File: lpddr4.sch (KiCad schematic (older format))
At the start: 41 parts

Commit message: Connect power supplies and CHANNEL A signals to edge connector
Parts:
- removed R?: R_240R_0402, lpddr4-testbed-footprints:0402-res, symbol lpddr4-testbed:R_240R_0402
- removed R? (x7): R_40R2_0402, lpddr4-testbed-footprints:0402-res, symbol lpddr4-testbed:R_40R2_0402
- removed R?: R_0R_0402, lpddr4-testbed-footprints:0402-res, symbol lpddr4-testbed:R_0R_0402
- gave numbers to parts that had none: 31
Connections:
- net labels removed: CA0_B, CA1_B, CA2_B, CA3_B, CA4_B, CA5_B, CKE0_B, DM2_N, DM3_N, DQ16, DQ17, DQ18, DQ19, DQ20, DQ21, DQ22, DQ23, DQ24, DQ25, DQ26, DQ27, DQ28, DQ29, DQ30, DQ31, DQS2_C, DQS2_T, DQS3_C, DQS3_T, ODT0_B, ODT1
- wire segments 190 -> 114

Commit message: Connect signals to DDR CHANNEL A
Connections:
- net labels added: CA_0A, CA_1A, CK_CA, CK_TA, CS0_A, DMI_0A, DMI_1A, DQ00_A, DQ01_A, DQ02_A, DQ03_A, DQ04_A, DQ05_A, DQ06_A, DQ07_A, DQ08_A, DQ09_A, DQ10_A, DQ11_A, DQ12_A, DQ13_A, DQ14_A, DQ15_A, DQ_S0_CA, DQ_S0_TA, DQ_S1_CA, DQ_S1_TA, VDD1, VDD2, VDDQ
- net labels removed: DM0_N, DM1_N, DQ00, DQ01, DQ02, DQ03, DQ04, DQ05, DQ06, DQ07, DQ08, DQ09, DQ10, DQ11, DQ12, DQ13, DQ14, DQ15, DQS0_C, DQS0_T, DQS1_C, DQS1_T
- wire segments 114 -> 120
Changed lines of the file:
@@
 $EndDescr
 Wire Wire Line
-	4650 5550 4650 5850
+	4650 5550 4650 5625
 $Comp
 L lpddr4-testbed:GND #PWR01
 U 1 1 6041895C
-P 4650 5850
-F 0 "#PWR01" H 4650 5600 50  0001 C CNN
-F 1 "GND" H 4655 5677 50  0000 C CNN
-F 2 "" H 4650 5850 50  0001 C CNN
-F 3 "" H 4650 5850 50  0001 C CNN
-	1    4650 5850
-	1    0    0    -1
-$EndComp
-Wire Wire Line
-	10900 5550 10900 5850
+P 4650 5625
+F 0 "#PWR01" H 4650 5375 50  0001 C CNN
+F 1 "GND" H 4655 5452 50  0000 C CNN
+F 2 "" H 4650 5625 50  0001 C CNN
+F 3 "" H 4650 5625 50  0001 C CNN
+	1    4650 5625
+	1    0    0    -1
+$EndComp
+Wire Wire Line
+	10900 5550 10900 5650
 $Comp
 L lpddr4-testbed:GND #PWR09
 U 1 1 6042116F
-P 10900 5850
-F 0 "#PWR09" H 10900 5600 50  0001 C CNN
-F 1 "GND" H 10905 5677 50  0000 C CNN
-F 2 "" H 10900 5850 50  0001 C CNN
-F 3 "" H 10900 5850 50  0001 C CNN
-	1    10900 5850
-	1    0    0    -1
-$EndComp
-Text Label 3050 4550 0    50   ~ 0
-DQ01
-Wire Wire Line
-	3050 4550 3850 4550
-Wire Wire Line
-	3050 4750 3850 4750
-Wire Wire Line
-	3050 4950 3850 4950
-Wire Wire Line
-	3850 5150 3050 5150
-Text Label 3050 4750 0    50   ~ 0
-DQ03
-Text Label 3050 4950 0    50   ~ 0
-DQ05
-Text Label 3050 5150 0    50   ~ 0
-DQ07
-Wire Wire Line
-	3850 4450 3050 4450
-Wire Wire Line
-	3850 4650 3050 4650
-Wire Wire Line
-	3850 4850 3050 4850
-Wire Wire Line
-	3850 5050 3050 5050
-Text Label 3050 4650 0    50   ~ 0
-DQ02
-Text Label 3050 4850 0    50   ~ 0
-DQ04
-Text Label 3050 5050 0    50   ~ 0
-DQ06
-Text Label 3050 4450 0    50   ~ 0
-DQ00
-Text Label 6250 5050 2    50   ~ 0
-DQ14
-Wire Wire Line
-	6250 5050 5450 5050
-Wire Wire Line
-	6250 4850 5450 4850
-Wire Wire Line
-	6250 4650 5450 4650
-Wire Wire Line
-	5450 4450 6250 4450
-Text Label 6250 4650 2    50   ~ 0
-DQ10
-Text Label 6250 4450 2    50   ~ 0
-DQ08
-Wire Wire Line
-	5450 5150 6250 5150
-Wire Wire Line
-	5450 4950 6250 4950
-Wire Wire Line
-	5450 4750 6250 4750
-Wire Wire Line
-	5450 4550 6250 4550
-Text Label 6250 4950 2    50   ~ 0
-DQ13
-Text Label 6250 4750 2    50   ~ 0
-DQ11
-Text Label 6250 4550 2    50   ~ 0
-DQ09
-Text Label 6250 5150 2    50   ~ 0
-DQ15
-Wire Wire Line
-	3050 4250 3850 4250
-Wire Wire Line
-	3850 4350 3050 4350
-Text Label 3050 4350 0    50   ~ 0
-DQS0_C
-Text Label 3050 4250 0    50   ~ 0
-DQS0_T
-Wire Wire Line
-	6250 4250 5450 4250
-Wire Wire Line
-	5450 4350 6250 4350
-Text Label 6250 4350 2    50   ~ 0
-DQS1_C
-Wire Wire Line
-	3850 5250 3050 5250
-Text Label 3050 5250 0    50   ~ 0
-DM0_N
-Wire Wire Line
-	5450 5250 6250 5250
-Text Label 6250 5250 2    50   ~ 0
-DM1_N
-Wire Wire Line
-	3850 3050 3050 3050
-Text Label 3050 3050 0    50   ~ 0
-CS0_N_A
+P 10900 5650
+F 0 "#PWR09" H 10900 5400 50  0001 C CNN
+F 1 "GND" H 10905 5477 50  0000 C CNN
+F 2 "" H 10900 5650 50  0001 C CNN
+F 3 "" H 10900 5650 50  0001 C CNN
+	1    10900 5650
+	1    0    0    -1
+$EndComp
 Wire Wire Line
 	5450 2850 6250 2850
 Text Label 6250 2850 2    50   ~ 0
 ODT0_A
-Text Label 6250 4250 2    50   ~ 0
-DQS1_T
-Wire Wire Line
-	3850 3950 3050 3950
-Text Label 3050 3950 0    50   ~ 0
-CKE0_A
 $Comp
 L lpddr4-testbed:C_100p_0402 C1
@@
 $EndComp
 Wire Wire Line
-	3850 3350 3050 3350
-Text Label 3050 3350 0    50   ~ 0
-CA0_A
-Text Label 3050 3450 0    50   ~ 0
-CA1_A
-Text Label 3050 3550 0    50   ~ 0
-CA2_A
-Text Label 3050 3650 0    50   ~ 0
-CA3_A
-Text Label 3050 3750 0    50   ~ 0
-CA4_A
-Text Label 3050 3850 0    50   ~ 0
-CA5_A
-Wire Wire Line
-	3850 3450 3050 3450
-Wire Wire Line
-	3850 3550 3050 3550
-Wire Wire Line
-	3850 3650 3050 3650
-Wire Wire Line
-	3850 3750 3050 3750
-Wire Wire Line
-	3850 3850 3050 3850
-Wire Wire Line
 	7450 7700 6650 7700
 Text Label 6650 7700 0    50   ~ 0
@@
 Text Label 3650 9275 0    50   ~ 0
 CK1_C
-Wire Wire Line
-	3050 2850 3850 2850
-Wire Wire Line
-	3850 2950 3050 2950
 $Comp
 L lpddr4-testbed:R_40R2_0402 R2
@@
 Wire Wire Line
 	3325 10150 3950 10150
-Text Label 3050 2950 0    50   ~ 0
-CK0_C
-Text Label 3050 2850 0    50   ~ 0
-CK0_T
 Text Notes 4875 10325 0    79   ~ 0
 OR
@@
 Text Notes 4625 7200 0    79   ~ 0
 DDR4
-Text Label 6250 4850 2    50   ~ 0
-DQ12
 Text GLabel 8275 6925 1    50   Input ~ 0
 DDRVCC
@@
 Wire Wire Line
 	7450 9450 7450 9725
+Wire Wire Line
+	5450 4750 5725 4750
+Text GLabel 5725 4750 2    50   Input ~ 0
+DQ11_A
+Wire Wire Line
+	5450 4650 5725 4650
+Text GLabel 5725 4650 2    50   Input ~ 0
+DQ10_A
+Wire Wire Line
+	5450 4550 5725 4550
+Text GLabel 5725 4550 2    50   Input ~ 0
+DQ09_A
+Wire Wire Line
+	5450 4450 5725 4450
+Text GLabel 5725 4450 2    50   Input ~ 0
+DQ08_A
+Wire Wire Line
+	5450 5250 5725 5250
+Text GLabel 5725 5250 2    50   Input ~ 0
+DMI_1A
+Wire Wire Line
+	5450 4350 5725 4350
+Text GLabel 5725 4350 2    50   Input ~ 0
+DQ_S1_CA
+Wire Wire Line
+	5450 4250 5725 4250
+Text GLabel 5725 4250 2    50   Input ~ 0
+DQ_S1_TA
+Wire Wire Line
+	5450 5150 5725 5150
+Text GLabel 5725 5150 2    50   Input ~ 0
+DQ15_A
+Wire Wire Line
+	5450 5050 5725 5050
+Text GLabel 5725 5050 2    50   Input ~ 0
+DQ14_A
+Wire Wire Line
+	5450 4950 5725 4950
+Text GLabel 5725 4950 2    50   Input ~ 0
+DQ13_A
+Wire Wire Line
+	5450 4850 5725 4850
+Text GLabel 5725 4850 2    50   Input ~ 0
+DQ12_A
+Wire Wire Line
+	3850 4850 3550 4850
+Text GLabel 3550 4850 0    50   Input ~ 0
+DQ04_A
+Wire Wire Line
+	3850 4950 3550 4950
+Text GLabel 3550 4950 0    50   Input ~ 0
+DQ05_A
+Wire Wire Line
+	3850 5050 3550 5050
+Text GLabel 3550 5050 0    50   Input ~ 0
+DQ06_A
+Wire Wire Line
+	3850 5250 3550 5250
+Text GLabel 3550 5250 0    50   Input ~ 0
+DMI_0A
+Wire Wire Line
+	3850 5150 3550 5150
+Text GLabel 3550 5150 0    50   Input ~ 0
+DQ07_A
+Wire Wire Line
+	3850 4250 3550 4250
+Text GLabel 3550 4250 0    50   Input ~ 0
+DQ_S0_TA
+Wire Wire Line
+	3850 4750 3550 4750
+Text GLabel 3550 4750 0    50   Input ~ 0
+DQ03_A
+Wire Wire Line
+	3850 4650 3550 4650
+Text GLabel 3550 4650 0    50   Input ~ 0
+DQ02_A
+Wire Wire Line
+	3850 4550 3550 4550
+Text GLabel 3550 4550 0    50   Input ~ 0
+DQ01_A
+Wire Wire Line
+	3850 4450 3550 4450
+Text GLabel 3550 4450 0    50   Input ~ 0
+DQ00_A
+Text GLabel 3550 3850 0    50   Input ~ 0
+CA5_A
+Wire Wire Line
+	3850 3850 3550 3850
+Text GLabel 3550 3750 0    50   Input ~ 0
+CA4_A
+Wire Wire Line
+	3850 3750 3550 3750
+Text GLabel 3550 3650 0    50   Input ~ 0
+CA3_A
+Wire Wire Line
+	3850 3650 3550 3650
+Text GLabel 3550 3550 0    50   Input ~ 0
+CA2_A
+Wire Wire Line
+	3850 3550 3550 3550
+Text GLabel 3175 2950 0    50   Input ~ 0
+CK_CA
+Wire Wire Line
+	3850 2950 3175 2950
+Text GLabel 3175 2850 0    50   Input ~ 0
+CK_TA
+Wire Wire Line
+	3850 2850 3175 2850
+Text GLabel 3175 3050 0    50   Input ~ 0
+CS0_A
+Wire Wire Line
+	3850 3050 3175 3050
+Text GLabel 3550 3950 0    50   Input ~ 0
+CKE0_A
+Wire Wire Line
+	3850 3950 3550 3950
+Text GLabel 3550 3350 0    50   Input ~ 0
+CA_0A
+Wire Wire Line
+	3850 3350 3550 3350
+Text GLabel 3550 3450 0    50   Input ~ 0
+CA_1A
+Wire Wire Line
+	3850 3450 3550 3450
+Text GLabel 3550 4350 0    50   Input ~ 0
+DQ_S0_CA
+Wire Wire Line
+	3850 4350 3550 4350
+Wire Wire Line
+	4550 2550 4550 2300
+Text GLabel 4550 2300 1    50   Input ~ 0
+VDD1
+Text GLabel 4750 2300 1    50   Input ~ 0
+VDDQ
+Wire Wire Line
+	4750 2550 4750 2300
+Wire Wire Line
+	4650 2550 4650 2300
+Text GLabel 4650 2300 1    50   Input ~ 0
+VDD2
+Wire Wire Line
+	10800 2550 10800 2300
+Text GLabel 10800 2300 1    50   Input ~ 0
+VDD1
+Text GLabel 11000 2300 1    50   Input ~ 0
+VDDQ
+Wire Wire Line
+	11000 2550 11000 2300
+Wire Wire Line
+	10900 2550 10900 2300
+Text GLabel 10900 2300 1    50   Input ~ 0
+VDD2
 $EndSCHEMATC

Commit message: Remove obsolete RC components around CK and CE signals
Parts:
- removed C1: C_100p_0402, lpddr4-testbed-footprints:0402-cap, symbol lpddr4-testbed:C_100p_0402
- removed C2: C_3p3_0402, lpddr4-testbed-footprints:0402-res, symbol lpddr4-testbed:C_3p3_0402
- removed C3: C_10n_0402, lpddr4-testbed-footprints:0402-cap, symbol lpddr4-testbed:C_10n_0402
- removed R1: R_120R_0402, lpddr4-testbed-footprints:0402-res, symbol lpddr4-testbed:R_120R_0402
- removed R10, R11, R12, R13, R14, R15, R16, R8, R9: R_0R_0402, lpddr4-testbed-footprints:0402-res, symbol lpddr4-testbed:R_0R_0402
- removed R17, R19, R2, R21, R22, R23, R24, R25, R26, R27, R3, R4, R5: R_40R2_0402, lpddr4-testbed-footprints:0402-res, symbol lpddr4-testbed:R_40R2_0402
- removed R18, R20: R_80R6_0402, lpddr4-testbed-footprints:0402-res, symbol lpddr4-testbed:R_80R6_0402
- removed R6: R_75R_0402, lpddr4-testbed-footprints:0402-res, symbol lpddr4-testbed:R_75R_0402
- removed R7: R_4k7_0402, lpddr4-testbed-footprints:0402-res, symbol lpddr4-testbed:R_4k7_0402
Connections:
- net labels removed: CA0_A, CA1_A, CK0_C, CK0_T, CK1_C, CK1_T, CKE_0, CKE_0_A, CKE_0_B, CKE_1, CS0_N_A, CS0_N_B, CS_0_N, CS_1_N, DDRVCC, MEMRST_N, ODT0, RESET_CONN_N
- wire segments 120 -> 41
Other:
- note removed: "DDR4"
- note removed: "OR"
- note removed: "Pull up or pull down?\n"
- note removed: "To check"
- note removed: "What is this resistor for?"

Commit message: Cleanup, add TODOs
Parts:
- added R? (x3): R_10k_0402, antmicro-footprints:0402-res, symbol antmicroResistors0402:R_10k_0402
- added R?: R_0R_0402, antmicro-footprints:0402-res, symbol antmicroResistors0402:R_0R_0402
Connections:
- net GND: now also R?.2
- net VDDQ: now also R?.1
- net CS0_B: now reaches U1.R4 (CS0_B)
- net CS0_B: now also R?.1
- net ODT0_A: no longer names the net of U1.G2 (ODT_CA_A)
- net ODT0_A: now also R?.1, R?.2
- new net ODT_CA_A: R?.2
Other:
- note added: "TODO: connect to FPGA IO"
- note added: "TODO\nAdd reset handling\nADD ODT/ZQ control"
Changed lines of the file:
@@
 	1    0    0    -1
 $EndComp
-Wire Wire Line
-	5450 2850 6250 2850
-Text Label 6250 2850 2    50   ~ 0
-ODT0_A
+Text Label 6675 2850 2    50   ~ 0
+ODT_CA_A
 Text Notes 1075 1025 0    98   ~ 20
 LPDDR4
@@
 Text GLabel 10900 2300 1    50   Input ~ 0
 VDD2
+Text Notes 2025 6625 0    98   ~ 20
+TODO\nAdd reset handling\nADD ODT/ZQ control
+Text GLabel 9350 3050 0    50   Input ~ 0
+CS0_B
+Wire Wire Line
+	9350 3050 9500 3050
+$Comp
+L antmicroResistors0402:R_10k_0402 R?
+U 1 1 5FD7BAFA
+P 9500 3400
+F 0 "R?" V 9455 3470 60  0000 L CNN
+F 1 "R_10k_0402" H 9500 3250 60  0001 C CNN
+F 2 "antmicro-footprints:0402-res" H 9700 3600 60  0001 L CNN
+F 3 "" H 9500 3400 50  0001 C CNN
+F 4 "VISHAY" H 9700 3800 60  0001 L CNN "Manufacturer"
+F 5 "CRCW040210K0FKEDHP" H 9700 3700 60  0001 L CNN "MPN"
+F 6 "10k" V 9553 3470 50  0000 L CNN "Val"
+	1    9500 3400
+	0    1    1    0
+$EndComp
+$Comp
+L lpddr4-testbed:GND #PWR?
+U 1 1 5FD7DCCA
+P 9500 3550
+F 0 "#PWR?" H 9500 3300 50  0001 C CNN
+F 1 "GND" H 9505 3377 50  0000 C CNN
+F 2 "" H 9500 3550 50  0001 C CNN
+F 3 "" H 9500 3550 50  0001 C CNN
+	1    9500 3550
+	1    0    0    -1
+$EndComp
+Wire Wire Line
+	9500 3250 9500 3050
+Connection ~ 9500 3050
+Wire Wire Line
+	9500 3050 10100 3050
+$Comp
+L antmicroResistors0402:R_10k_0402 R?
+U 1 1 5FD80AED
+P 12000 3350
+F 0 "R?" V 11955 3420 60  0000 L CNN
+F 1 "R_10k_0402" H 12000 3200 60  0001 C CNN
+F 2 "antmicro-footprints:0402-res" H 12200 3550 60  0001 L CNN
+F 3 "" H 12000 3350 50  0001 C CNN
+F 4 "VISHAY" H 12200 3750 60  0001 L CNN "Manufacturer"
+F 5 "CRCW040210K0FKEDHP" H 12200 3650 60  0001 L CNN "MPN"
+F 6 "10k" V 12053 3420 50  0000 L CNN "Val"
+	1    12000 3350
+	0    1    1    0
+$EndComp
+$Comp
+L antmicroResistors0402:R_10k_0402 R?
+U 1 1 5FD814A6
+P 5625 2600
+F 0 "R?" V 5580 2670 60  0000 L CNN
+F 1 "R_10k_0402" H 5625 2450 60  0001 C CNN
+F 2 "antmicro-footprints:0402-res" H 5825 2800 60  0001 L CNN
+F 3 "" H 5625 2600 50  0001 C CNN
+F 4 "VISHAY" H 5825 3000 60  0001 L CNN "Manufacturer"
+F 5 "CRCW040210K0FKEDHP" H 5825 2900 60  0001 L CNN "MPN"
+F 6 "10k" V 5678 2670 50  0000 L CNN "Val"
+	1    5625 2600
+	0    1    1    0
+$EndComp
+Wire Wire Line
+	5625 2750 5625 2850
+Wire Wire Line
+	5450 2850 5625 2850
+Connection ~ 5625 2850
+Wire Wire Line
+	5625 2850 5875 2850
+Wire Wire Line
+	5625 2300 5625 2450
+Text GLabel 5625 2300 1    50   Input ~ 0
+VDDQ
+$Comp
+L antmicroResistors0402:R_0R_0402 R?
+U 1 1 5FD86989
+P 6025 2850
+F 0 "R?" H 6025 3063 60  0000 C CNN
+F 1 "R_0R_0402" H 6025 2700 60  0001 C CNN
+F 2 "antmicro-footprints:0402-res" H 6225 3050 60  0001 L CNN
+F 3 "" H 6025 2850 50  0001 C CNN
+F 4 "PANASONIC" H 6225 3250 60  0001 L CNN "Manufacturer"
+F 5 "ERJ2GE0R00X" H 6225 3150 60  0001 L CNN "MPN"
+F 6 "0R" H 6025 2965 50  0000 C CNN "Val"
+	1    6025 2850
+	1    0    0    -1
+$EndComp
+Wire Wire Line
+	6175 2850 6675 2850
+Text Notes 5750 3075 0    98   ~ 20
+TODO: connect to FPGA IO
+Text Notes 11900 3000 0    98   ~ 20
+TODO: connect to FPGA IO
 $EndSCHEMATC

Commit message: Add filtering caps to VDDQ
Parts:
- added C1, C10, C11, C12, C13, C15, C2, C3, C4, C5, C6, C7, C8, C9: C_100n_0201, antmicro-footprints:0201-res, symbol antmicroCapacitorsmisc:C_100n_0201
- gave numbers to parts that had none: 4
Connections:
- net GND: now also C1.2, C10.2, C11.2, C12.2, C13.2, C15.2, C2.2, C3.2, C4.2, C5.2, C6.2, C7.2, C8.2, C9.2
- net VDDQ: now also C1.1, C10.1, C11.1, C12.1, C13.1, C15.1, C2.1, C3.1, C4.1, C5.1, C6.1, C7.1, C8.1, C9.1

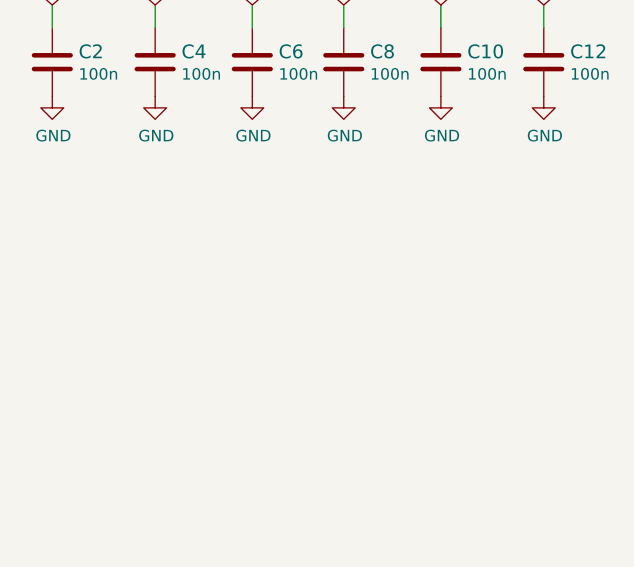
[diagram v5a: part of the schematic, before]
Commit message: Add Filtering to VCC1
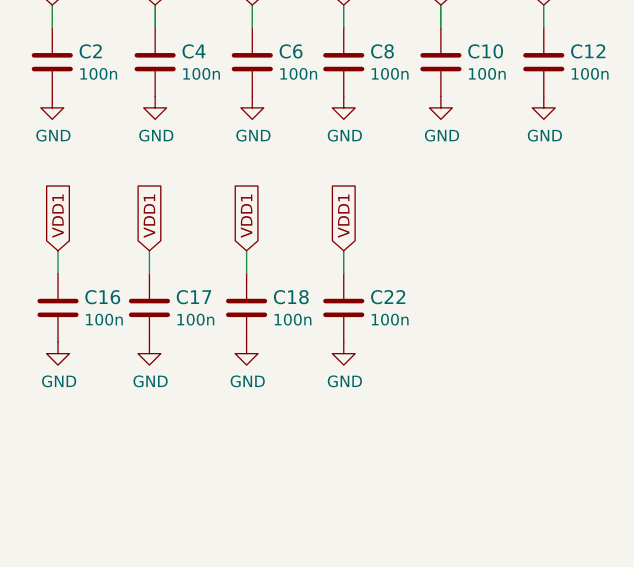
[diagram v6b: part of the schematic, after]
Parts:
- added C16, C17, C18, C22: C_100n_0201, antmicro-footprints:0201-res, symbol antmicroCapacitorsmisc:C_100n_0201
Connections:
- net GND: now also C16.2, C17.2, C18.2, C22.2
- net VDD1: now also C16.1, C17.1, C18.1, C22.1
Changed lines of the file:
@@
 Wire Wire Line
 	3375 8650 3375 8750
+$Comp
+L antmicroCapacitorsmisc:C_100n_0201 C16
+U 1 1 5FE0B8F2
+P 1250 9975
+F 0 "C16" H 1365 10020 60  0000 L CNN
+F 1 "C_100n_0201" H 1250 9825 60  0001 C CNN
+F 2 "antmicro-footprints:0201-res" H 1450 10175 60  0001 L CNN
+F 3 "" H 1250 9975 50  0001 C CNN
+F 4 "YAGEO" H 1450 10375 60  0001 L CNN "Manufacturer"
+F 5 "CC0201KRX6S5BB104" H 1450 10275 60  0001 L CNN "MPN"
+F 6 "100n" H 1365 9922 50  0000 L CNN "Val"
+	1    1250 9975
+	1    0    0    -1
+$EndComp
+$Comp
+L lpddr4-testbed:GND #PWR019
+U 1 1 5FE0B8F8
+P 1250 10125
+F 0 "#PWR019" H 1250 9875 50  0001 C CNN
+F 1 "GND" H 1255 9952 50  0000 C CNN
+F 2 "" H 1250 10125 50  0001 C CNN
+F 3 "" H 1250 10125 50  0001 C CNN
+	1    1250 10125
+	1    0    0    -1
+$EndComp
+Text GLabel 1250 9725 1    50   Input ~ 0
+VDD1
+Wire Wire Line
+	1250 9825 1250 9725
+$Comp
+L antmicroCapacitorsmisc:C_100n_0201 C17
+U 1 1 5FE0E056
+P 1650 9975
+F 0 "C17" H 1765 10020 60  0000 L CNN
+F 1 "C_100n_0201" H 1650 9825 60  0001 C CNN
+F 2 "antmicro-footprints:0201-res" H 1850 10175 60  0001 L CNN
+F 3 "" H 1650 9975 50  0001 C CNN
+F 4 "YAGEO" H 1850 10375 60  0001 L CNN "Manufacturer"
+F 5 "CC0201KRX6S5BB104" H 1850 10275 60  0001 L CNN "MPN"
+F 6 "100n" H 1765 9922 50  0000 L CNN "Val"
+	1    1650 9975
+	1    0    0    -1
+$EndComp
+$Comp
+L lpddr4-testbed:GND #PWR020
+U 1 1 5FE0E05C
+P 1650 10125
+F 0 "#PWR020" H 1650 9875 50  0001 C CNN
+F 1 "GND" H 1655 9952 50  0000 C CNN
+F 2 "" H 1650 10125 50  0001 C CNN
+F 3 "" H 1650 10125 50  0001 C CNN
+	1    1650 10125
+	1    0    0    -1
+$EndComp
+Text GLabel 1650 9725 1    50   Input ~ 0
+VDD1
+Wire Wire Line
+	1650 9825 1650 9725
+$Comp
+L antmicroCapacitorsmisc:C_100n_0201 C18
+U 1 1 5FE0E067
+P 2075 9975
+F 0 "C18" H 2190 10020 60  0000 L CNN
+F 1 "C_100n_0201" H 2075 9825 60  0001 C CNN
+F 2 "antmicro-footprints:0201-res" H 2275 10175 60  0001 L CNN
+F 3 "" H 2075 9975 50  0001 C CNN
+F 4 "YAGEO" H 2275 10375 60  0001 L CNN "Manufacturer"
+F 5 "CC0201KRX6S5BB104" H 2275 10275 60  0001 L CNN "MPN"
+F 6 "100n" H 2190 9922 50  0000 L CNN "Val"
+	1    2075 9975
+	1    0    0    -1
+$EndComp
+$Comp
+L lpddr4-testbed:GND #PWR021
+U 1 1 5FE0E06D
+P 2075 10125
+F 0 "#PWR021" H 2075 9875 50  0001 C CNN
+F 1 "GND" H 2080 9952 50  0000 C CNN
+F 2 "" H 2075 10125 50  0001 C CNN
+F 3 "" H 2075 10125 50  0001 C CNN
+	1    2075 10125
+	1    0    0    -1
+$EndComp
+Text GLabel 2075 9725 1    50   Input ~ 0
+VDD1
+Wire Wire Line
+	2075 9825 2075 9725
+$Comp
+L antmicroCapacitorsmisc:C_100n_0201 C22
+U 1 1 5FE11700
+P 2500 9975
+F 0 "C22" H 2615 10020 60  0000 L CNN
+F 1 "C_100n_0201" H 2500 9825 60  0001 C CNN
+F 2 "antmicro-footprints:0201-res" H 2700 10175 60  0001 L CNN
+F 3 "" H 2500 9975 50  0001 C CNN
+F 4 "YAGEO" H 2700 10375 60  0001 L CNN "Manufacturer"
+F 5 "CC0201KRX6S5BB104" H 2700 10275 60  0001 L CNN "MPN"
+F 6 "100n" H 2615 9922 50  0000 L CNN "Val"
+	1    2500 9975
+	1    0    0    -1
+$EndComp
+$Comp
+L lpddr4-testbed:GND #PWR025
+U 1 1 5FE11706
+P 2500 10125
+F 0 "#PWR025" H 2500 9875 50  0001 C CNN
+F 1 "GND" H 2505 9952 50  0000 C CNN
+F 2 "" H 2500 10125 50  0001 C CNN
+F 3 "" H 2500 10125 50  0001 C CNN
+	1    2500 10125
+	1    0    0    -1
+$EndComp
+Text GLabel 2500 9725 1    50   Input ~ 0
+VDD1
+Wire Wire Line
+	2500 9825 2500 9725
 $EndSCHEMATC
